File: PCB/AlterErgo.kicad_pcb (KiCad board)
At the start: 2 copper layers, 104 parts, among them J1 GS3, J2 SJ-43514, J3 GS3, J4 Conn_01x02, SW0:10 SW_Push, SW0:11 SW_Push, SW0:12 SW_Push, SW0:7 SW_Push, SW0:8 SW_Push, SW0:9 SW_Push, SW1 SW_SPST, SW1:10 SW_Push, SW1:11 SW_Push, SW1:12 SW_Push, SW1:13 SW_Push, SW1:7 SW_Push, SW1:8 SW_Push, SW1:9 SW_Push, SW2:10 SW_Push, SW2:11 SW_Push, SW2:12 SW_Push, SW2:13 SW_Push, SW2:7 SW_Push, SW2:8 SW_Push, SW2:9 SW_Push, SW3:10 SW_Push, SW3:11 SW_Push, SW3:12 SW_Push, SW3:13 SW_Push, SW3:8 SW_Push, SW3:9 SW_Push, SW4:10 SW_Push, SW4:11 SW_Push, SW4:12 SW_Push, SW4:13 SW_Push, SW4:7 SW_Push, SW4:8 SW_Push, SW4:9 SW_Push, SW5:10 SW_Push, SW5:11 SW_Push, SW5:12 SW_Push, SW5:13 SW_Push, SW5:7 SW_Push, SW5:8 SW_Push, SW5:9 SW_Push, U1 Feather32u4Bluefruit, U2 MCP23018

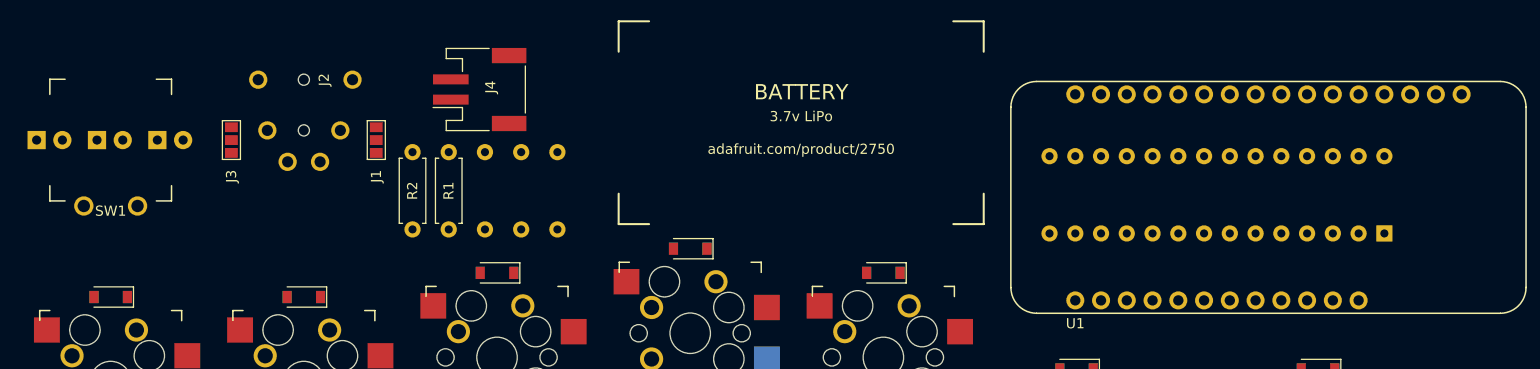
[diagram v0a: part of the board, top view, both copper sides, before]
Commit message: Initial attempt at routing traces in upper area
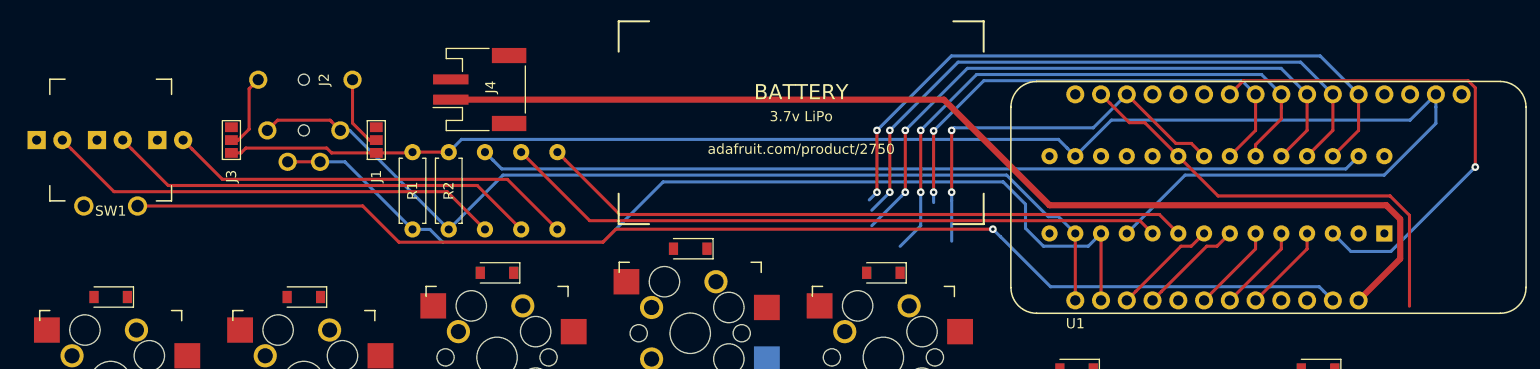
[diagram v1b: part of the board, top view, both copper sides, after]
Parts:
- moved R3 7.14 mm to (125.0, 42.1)
- moved R5 7.14 mm to (117.9, 42.1)
- moved R1 3.57 mm to (110.7, 34.5)
- moved R2 3.57 mm to (114.3, 34.5)
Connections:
- U2 pad 10: Net-(R3-Pad2) -> Net-(R4-Pad2)
- U2 pad 9: Net-(R4-Pad2) -> Net-(R3-Pad2)
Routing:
- net +3V3: track 0.00 -> 160.8 mm
- net Net-(SW1-Pad2): track 0.00 -> 122.8 mm, vias 0 -> 1
- net Net-(J4-Pad1): track 0.00 -> 108.2 mm
- net /SCL: track 0.00 -> 97.1 mm
- net /SDA: track 0.00 -> 95.8 mm
- net Net-(R5-Pad2): track 0.00 -> 87.4 mm
- net /COL6: track 0.00 -> 66.4 mm, vias 0 -> 2
- net Net-(R4-Pad2): track 0.00 -> 65.6 mm
- net Net-(R3-Pad2): track 0.00 -> 64.6 mm
- net /COL5: track 0.00 -> 63.5 mm, vias 0 -> 2
- net /COL4: track 0.00 -> 61.1 mm, vias 0 -> 2
- net /COL10: track 0.00 -> 58.1 mm, vias 0 -> 2
- net /ROW5: track 0.00 -> 51.1 mm, vias 0 -> 1
- net /COL11: track 0.00 -> 48.6 mm, vias 0 -> 2
- net Net-(D3-Pad2): track 0.00 -> 45.3 mm
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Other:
- net class Batt added: clearance 0.4572, trace_width 0.6096, via_dia 0.9144, via_drill 0.4572
- net class Default: clearance 0.1524 -> 0.3048; trace_width 0.1524 -> 0.3048; via_dia 0.6858 -> 0.762
- rule trace_clearance: 0.1524 -> 0.3048

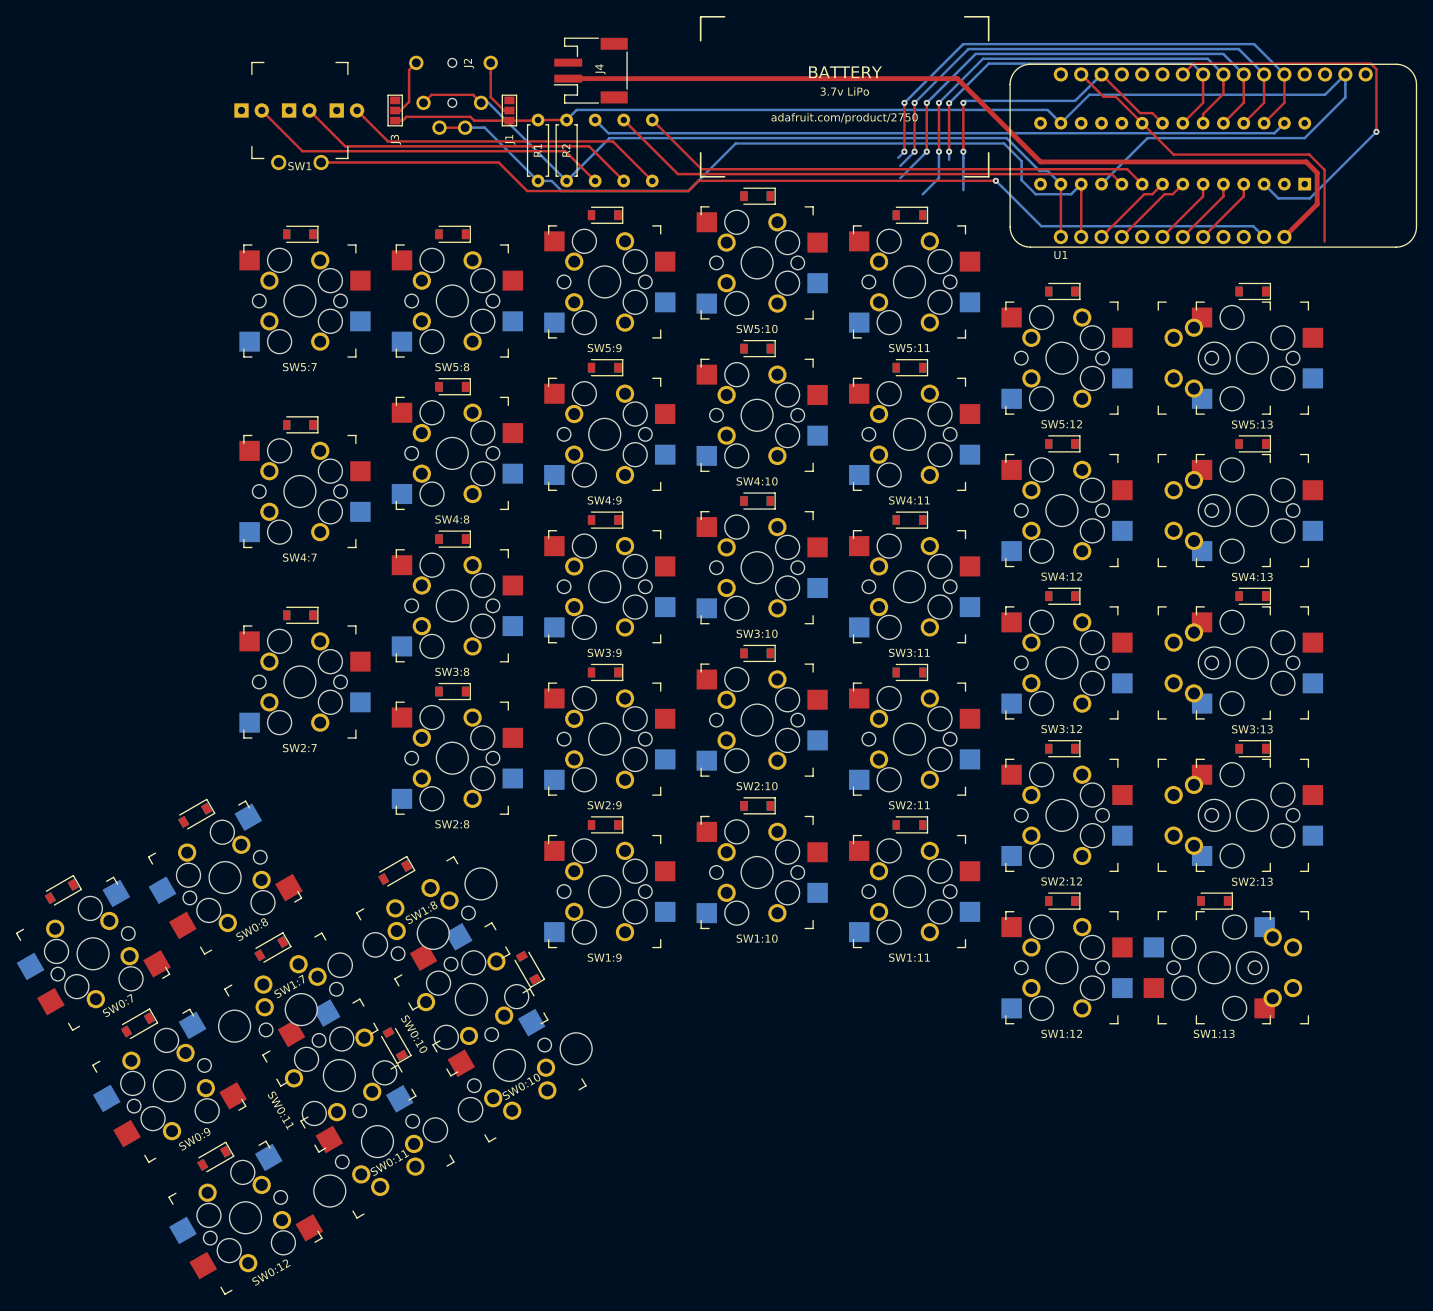
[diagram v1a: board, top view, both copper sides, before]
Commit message: Route columns
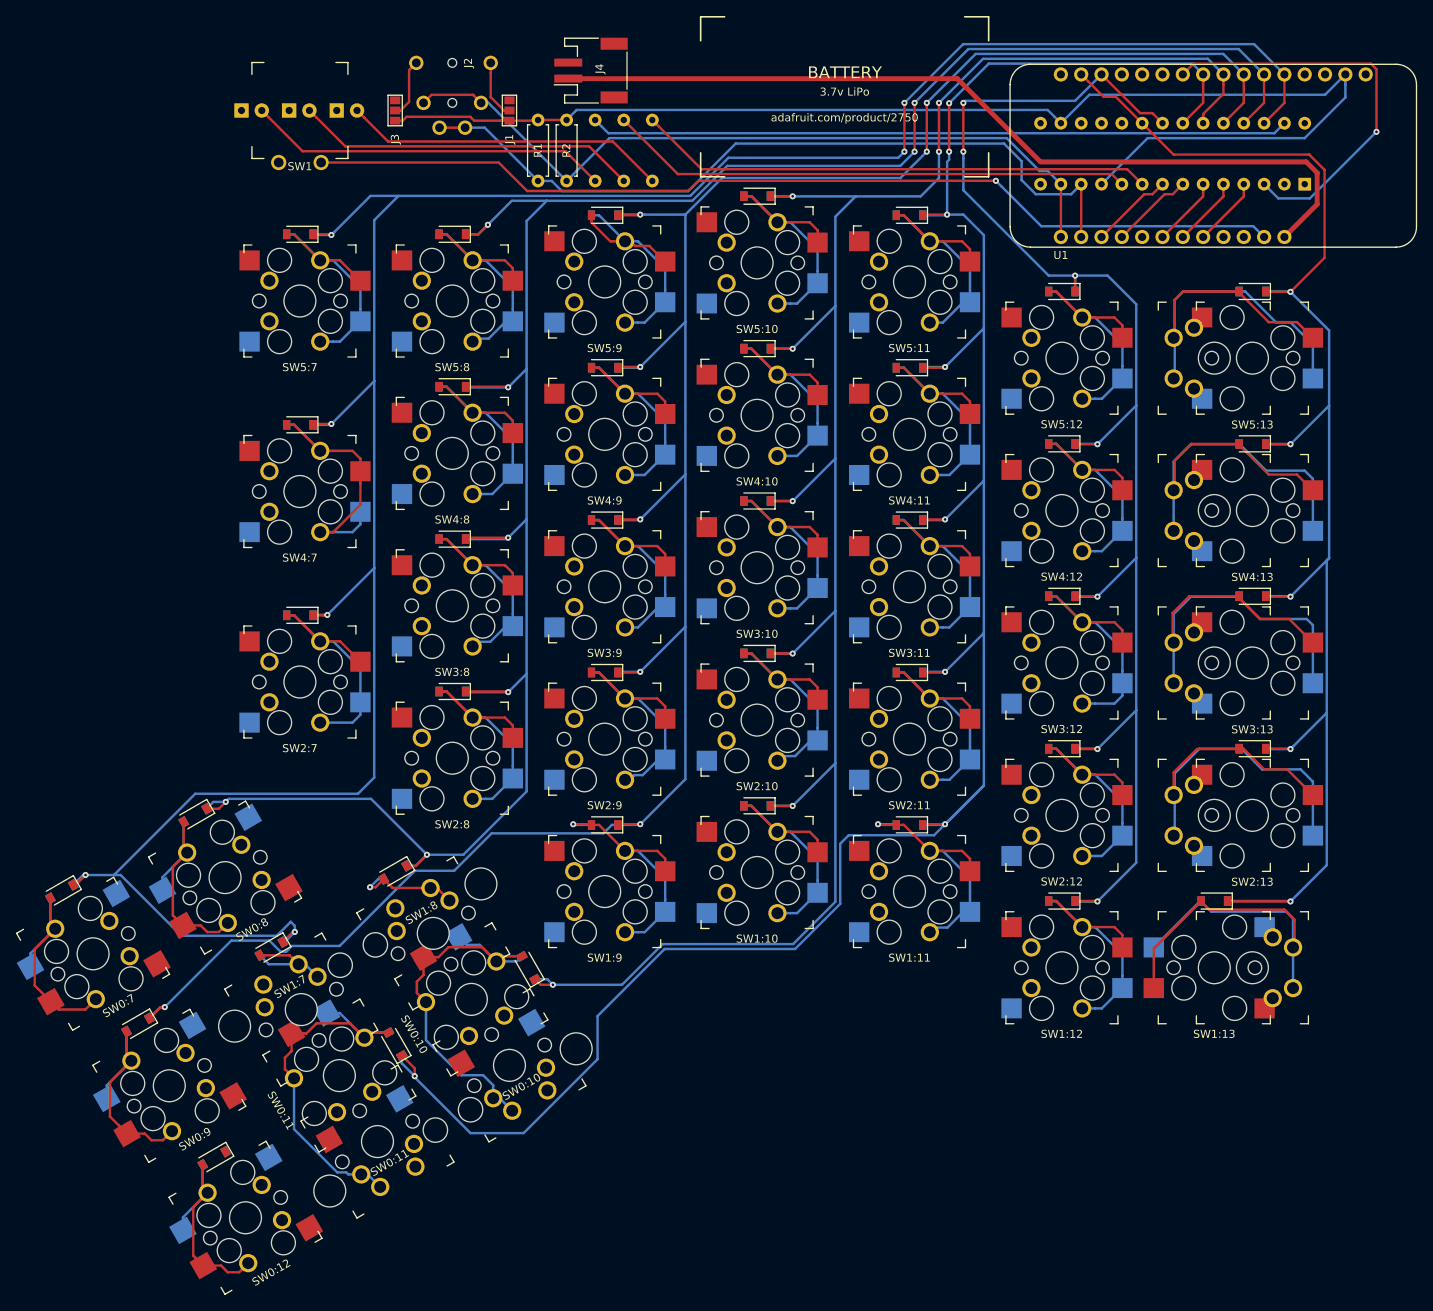
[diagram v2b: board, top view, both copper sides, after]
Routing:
- net /COL6: track 66.4 -> 320.8 mm, vias 2 -> 7
- net /COL11: track 48.6 -> 292.5 mm, vias 2 -> 8
- net /COL4: track 61.1 -> 298.5 mm, vias 2 -> 8
- net /COL5: track 63.5 -> 297.4 mm, vias 2 -> 8
- net /COL10: track 58.1 -> 266.5 mm, vias 2 -> 8
- net /COL1: track 39.8 -> 191.0 mm, vias 2 -> 7
- net /COL0: track 44.3 -> 193.5 mm, vias 0 -> 5
- net (no net): track 0.00 -> 69.1 mm
- net Net-(D5:13-Pad2): track 0.00 -> 59.1 mm
- net Net-(D0:10-Pad2): track 0.00 -> 49.8 mm
- net Net-(D0:11-Pad2): track 0.00 -> 49.5 mm
- net Net-(D2:13-Pad2): track 0.00 -> 46.5 mm
- net Net-(D3:13-Pad2): track 0.00 -> 42.9 mm
- net Net-(D4:13-Pad2): track 0.00 -> 42.2 mm
- net Net-(D1:13-Pad2): track 0.00 -> 37.9 mm
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
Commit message: Route rows
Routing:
- net /ROW0: track 10.4 -> 361.2 mm, vias 0 -> 2
- net /ROW1: track 10.4 -> 360.6 mm, vias 0 -> 2
- net /ROW2: track 8.71 -> 326.2 mm, vias 0 -> 2
- net /ROW5: track 51.1 -> 322.2 mm, vias 1 -> 2
- net /ROW4: track 8.71 -> 279.7 mm, vias 0 -> 1
- net /ROW3: track 8.71 -> 276.8 mm, vias 0 -> 2
- net /COL1: track 191.0 -> 327.5 mm, vias 7 -> 8
- net (no net): track 69.1 -> 98.3 mm
- net /COL10: track 266.5 -> 262.8 mm, vias 8 -> 9
- net /COL6: track 320.8 -> 318.6 mm
